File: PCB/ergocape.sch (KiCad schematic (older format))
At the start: 90 parts, among them J1 AudioJack4, J2 AudioJack4, SW1 SW_PUSH, U1 ATMEGA32U4, X1 Crystal_GND24_Small

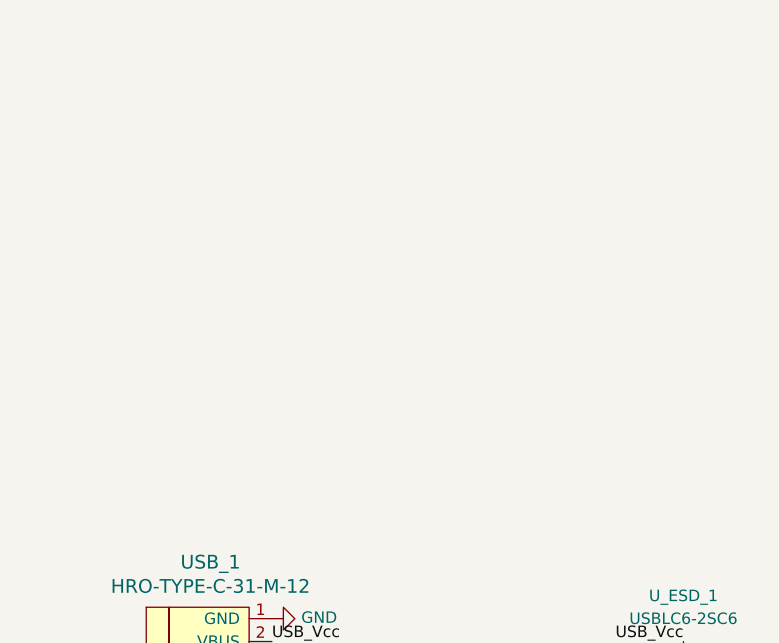
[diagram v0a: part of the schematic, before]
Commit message: added files for case files based of fr4 or similar.
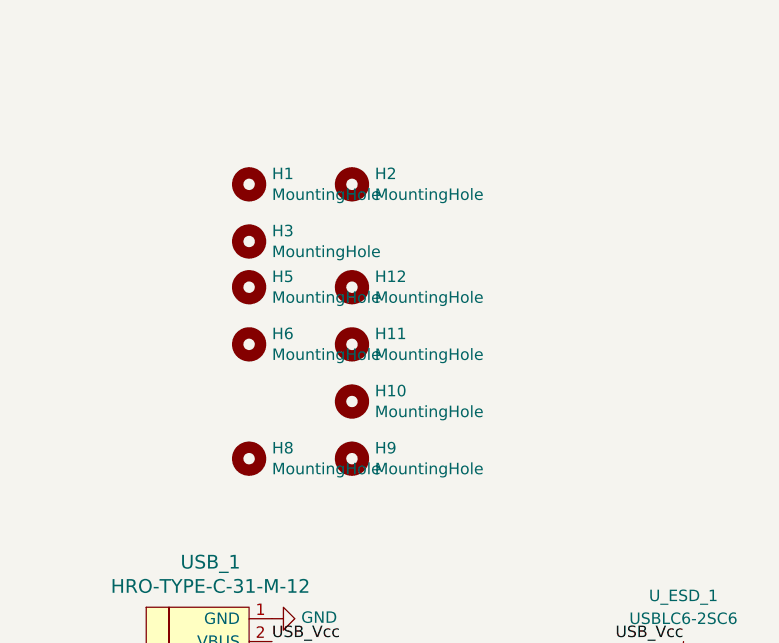
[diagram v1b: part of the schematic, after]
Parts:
- added H1, H10, H11, H12, H2, H3, H5, H6, H8, H9: MountingHole, usbc_footprint:mounting_hole_4.7x5.2mm, symbol Mechanical:MountingHole
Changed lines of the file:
@@
 $EndComp
 $Comp
-L power:GND #PWR?
+L power:GND #PWR0101
 U 1 1 5E0EA927
 P 8700 4250
-F 0 "#PWR?" H 8700 4000 50  0001 C CNN
+F 0 "#PWR0101" H 8700 4000 50  0001 C CNN
 F 1 "GND" H 8705 4077 50  0000 C CNN
 F 2 "" H 8700 4250 50  0001 C CNN
@@
 	4500 2900 4500 3400
 $Comp
-L power:GND #PWR?
+L power:GND #PWR0127
 U 1 1 5E1077CE
 P 2900 7500
-F 0 "#PWR?" H 2900 7250 50  0001 C CNN
+F 0 "#PWR0127" H 2900 7250 50  0001 C CNN
 F 1 "GND" V 2905 7372 50  0000 R CNN
 F 2 "" H 2900 7500 50  0001 C CNN
@@
 	1    0    0    -1
 $EndComp
+$Comp
+L Mechanical:MountingHole H5
+U 1 1 5E126410
+P 1000 4950
+F 0 "H5" H 1100 4996 50  0000 L CNN
+F 1 "MountingHole" H 1100 4905 50  0000 L CNN
+F 2 "usbc_footprint:mounting_hole_4.7x5.2mm" H 1000 4950 50  0001 C CNN
+F 3 "~" H 1000 4950 50  0001 C CNN
+	1    1000 4950
+	1    0    0    -1
+$EndComp
+$Comp
+L Mechanical:MountingHole H12
+U 1 1 5E12675F
+P 1450 4950
+F 0 "H12" H 1550 4996 50  0000 L CNN
+F 1 "MountingHole" H 1550 4905 50  0000 L CNN
+F 2 "usbc_footprint:mounting_hole_4.7x5.2mm" H 1450 4950 50  0001 C CNN
+F 3 "~" H 1450 4950 50  0001 C CNN
+	1    1450 4950
+	1    0    0    -1
+$EndComp
+$Comp
+L Mechanical:MountingHole H6
+U 1 1 5E12F4CE
+P 1000 5200
+F 0 "H6" H 1100 5246 50  0000 L CNN
+F 1 "MountingHole" H 1100 5155 50  0000 L CNN
+F 2 "usbc_footprint:mounting_hole_4.7x5.2mm" H 1000 5200 50  0001 C CNN
+F 3 "~" H 1000 5200 50  0001 C CNN
+	1    1000 5200
+	1    0    0    -1
+$EndComp
+$Comp
+L Mechanical:MountingHole H11
+U 1 1 5E12F4D5
+P 1450 5200
+F 0 "H11" H 1550 5246 50  0000 L CNN
+F 1 "MountingHole" H 1550 5155 50  0000 L CNN
+F 2 "usbc_footprint:mounting_hole_4.7x5.2mm" H 1450 5200 50  0001 C CNN
+F 3 "~" H 1450 5200 50  0001 C CNN
+	1    1450 5200
+	1    0    0    -1
+$EndComp
+$Comp
+L Mechanical:MountingHole H10
+U 1 1 5E138366
+P 1450 5450
+F 0 "H10" H 1550 5496 50  0000 L CNN
+F 1 "MountingHole" H 1550 5405 50  0000 L CNN
+F 2 "usbc_footprint:mounting_hole_4.7x5.2mm" H 1450 5450 50  0001 C CNN
+F 3 "~" H 1450 5450 50  0001 C CNN
+	1    1450 5450
+	1    0    0    -1
+$EndComp
+$Comp
+L Mechanical:MountingHole H8
+U 1 1 5E13836D
+P 1000 5700
+F 0 "H8" H 1100 5746 50  0000 L CNN
+F 1 "MountingHole" H 1100 5655 50  0000 L CNN
+F 2 "usbc_footprint:mounting_hole_4.7x5.2mm" H 1000 5700 50  0001 C CNN
+F 3 "~" H 1000 5700 50  0001 C CNN
+	1    1000 5700
+	1    0    0    -1
+$EndComp
+$Comp
+L Mechanical:MountingHole H9
+U 1 1 5E138374
+P 1450 5700
+F 0 "H9" H 1550 5746 50  0000 L CNN
+F 1 "MountingHole" H 1550 5655 50  0000 L CNN
+F 2 "usbc_footprint:mounting_hole_4.7x5.2mm" H 1450 5700 50  0001 C CNN
+F 3 "~" H 1450 5700 50  0001 C CNN
+	1    1450 5700
+	1    0    0    -1
+$EndComp
+$Comp
+L Mechanical:MountingHole H1
+U 1 1 5E1411A4
+P 1000 4500
+F 0 "H1" H 1100 4546 50  0000 L CNN
+F 1 "MountingHole" H 1100 4455 50  0000 L CNN
+F 2 "usbc_footprint:mounting_hole_4.7x5.2mm" H 1000 4500 50  0001 C CNN
+F 3 "~" H 1000 4500 50  0001 C CNN
+	1    1000 4500
+	1    0    0    -1
+$EndComp
+$Comp
+L Mechanical:MountingHole H2
+U 1 1 5E1411AB
+P 1450 4500
+F 0 "H2" H 1550 4546 50  0000 L CNN
+F 1 "MountingHole" H 1550 4455 50  0000 L CNN
+F 2 "usbc_footprint:mounting_hole_4.7x5.2mm" H 1450 4500 50  0001 C CNN
+F 3 "~" H 1450 4500 50  0001 C CNN
+	1    1450 4500
+	1    0    0    -1
+$EndComp
+$Comp
+L Mechanical:MountingHole H3
+U 1 1 5E1411B2
+P 1000 4750
+F 0 "H3" H 1100 4796 50  0000 L CNN
+F 1 "MountingHole" H 1100 4705 50  0000 L CNN
+F 2 "usbc_footprint:mounting_hole_4.7x5.2mm" H 1000 4750 50  0001 C CNN
+F 3 "~" H 1000 4750 50  0001 C CNN
+	1    1000 4750
+	1    0    0    -1
+$EndComp

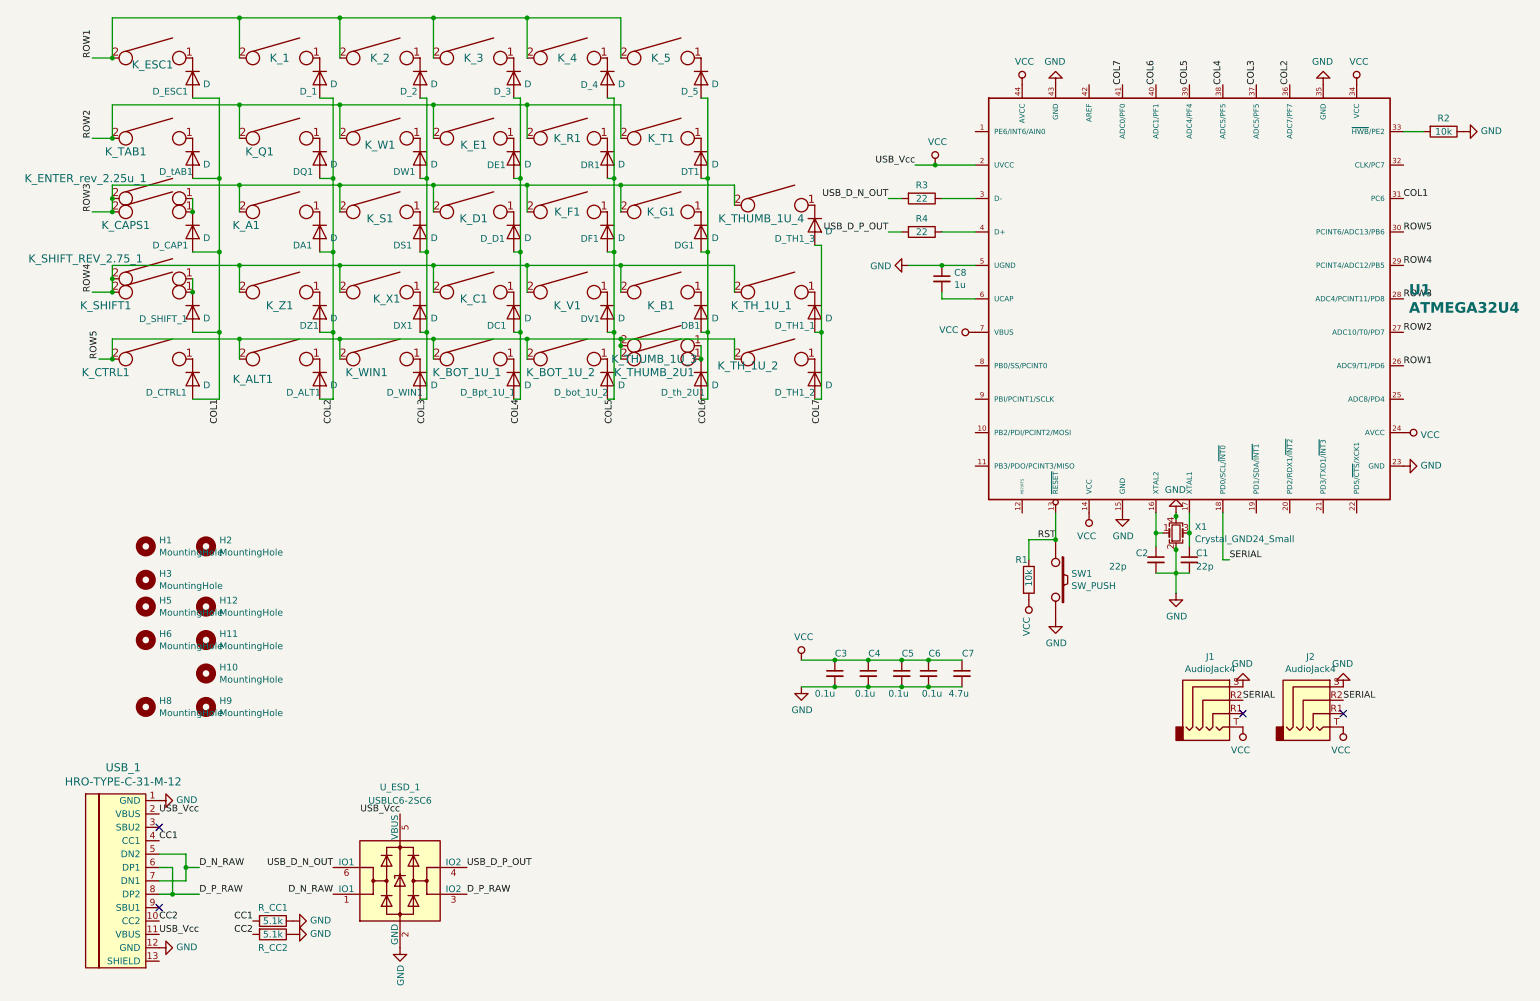
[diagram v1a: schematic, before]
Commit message: Change in layout and design, remove atmega32u4
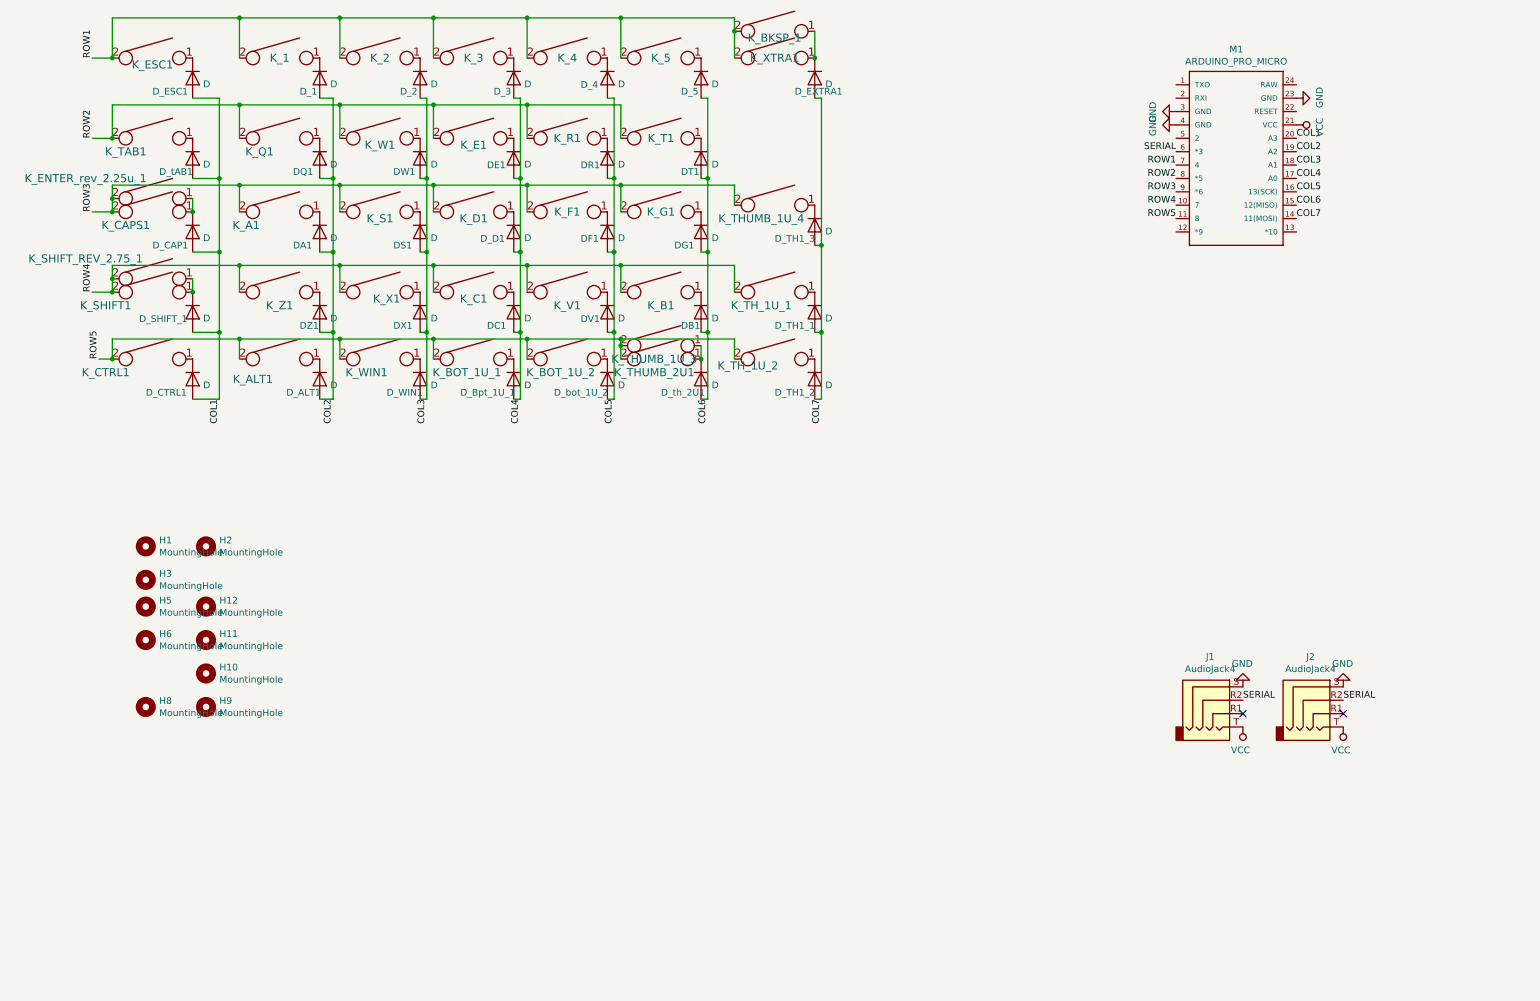
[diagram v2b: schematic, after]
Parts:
- removed C1, C2: 22p, Capacitor_SMD:C_0805_2012Metric_Pad1.15x1.40mm_HandSolder, symbol Device:C_Small
- removed C3, C4, C5, C6: 0.1u, Capacitor_SMD:C_0805_2012Metric_Pad1.15x1.40mm_HandSolder, symbol Device:C_Small
- removed C7: 4.7u, Capacitor_SMD:C_0805_2012Metric_Pad1.15x1.40mm_HandSolder, symbol Device:C_Small
- removed C8: 1u, Capacitor_SMD:C_0805_2012Metric_Pad1.15x1.40mm_HandSolder, symbol Device:C_Small
- removed R1, R2: 10k, Resistor_SMD:R_0805_2012Metric_Pad1.15x1.40mm_HandSolder, symbol Device:R
- removed R3, R4: 22, Resistor_SMD:R_0805_2012Metric_Pad1.15x1.40mm_HandSolder, symbol Device:R
- removed R_CC1, R_CC2: 5.1k, Resistor_SMD:R_0805_2012Metric_Pad1.15x1.40mm_HandSolder, symbol Device:R
- removed SW1: SW_PUSH, Button_Switch_SMD:SW_SPST_TL3342, symbol keyboard_parts:SW_PUSH
- removed U1: ATMEGA32U4, acheron_Components:TQPF-44_10x10mm_P0.8mm, symbol ergocape-rescue:ATMEGA32U4-acheronSymbols
- removed USB_1: HRO-TYPE-C-31-M-12, usbc_footprint:HRO-TYPE-C-31-M-12, symbol Type-C:HRO-TYPE-C-31-M-12
- removed U_ESD_1: USBLC6-2SC6, Package_TO_SOT_SMD:SOT-23-6, symbol Power_Protection_esd:USBLC6-2SC6
- removed X1: Crystal_GND24_Small, acheron_Components:Crystal_SMD_5032-4Pin-HandSolder, symbol Device:Crystal_GND24_Small
- added D_EXTRA1: D, Keebio-Parts:Diode-dual, symbol Device:D
- added K_BKSP_1: KEYSW, Keebio-Parts:Hybrid_PCB_200H-dual, symbol keyboard_parts:KEYSW
- added K_XTRA1: KEYSW, Keebio-Parts:Hybrid_PCB_100H_Dual_hole, symbol keyboard_parts:KEYSW
- added M1: ARDUINO_PRO_MICRO, SparkFun-Boards:ARDUINO_PRO_MICRO, symbol SparkFun-Boards:ARDUINO_PRO_MICRO
- H1, H10, H11, H12, H2, H3, H5, H6, H8, H9: footprint usbc_footprint:mounting_hole_4.7x5.2mm -> acheron_MountingHoles:MountingHole_2.5x4.0mm
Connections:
- net COL1: now also M1.20 (A3)
- net COL2: now also M1.19 (A2)
- net COL3: now also M1.18 (A1)
- net COL4: now also M1.17 (A0)
- net COL5: now also M1.16 (13(SCK))
- net COL6: now also M1.15 (12(MISO))
- net COL7: now also D_EXTRA1.2 (A), M1.14 (11(MOSI))
- net GND: now also M1.23 (GND), M1.3 (GND), M1.4 (GND)
- net ROW1: now also K_BKSP_1.2, K_XTRA1.2, M1.7 (4)
- net ROW2: now also M1.8 (*5)
- net ROW3: now also M1.9 (*6)
- net ROW4: now also M1.10 (7)
- net ROW5: now also M1.11 (8)
- net SERIAL: now also M1.6 (*3)
- net VCC: now also M1.21 (VCC)
- new net: D_EXTRA1.1 (K), K_BKSP_1.1, K_XTRA1.1
- no-connect marks 4 -> 2

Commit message: finalize plate and mounting holes
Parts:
- H1, H10, H11, H12, H2, H3, H5, H6, H8, H9: footprint acheron_MountingHoles:MountingHole_2.5x4.0mm -> usbc_footprint:mounting_hole_4.7x5.2mm
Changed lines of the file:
@@
 EESchema Schematic File Version 4
-LIBS:ergocape-cache
-EELAYER 26 0
+EELAYER 30 0
 EELAYER END
 $Descr A4 11693 8268
@@
 F 0 "H5" H 1100 4996 50  0000 L CNN
 F 1 "MountingHole" H 1100 4905 50  0000 L CNN
-F 2 "acheron_MountingHoles:MountingHole_2.5x4.0mm" H 1000 4950 50  0001 C CNN
+F 2 "usbc_footprint:mounting_hole_4.7x5.2mm" H 1000 4950 50  0001 C CNN
 F 3 "~" H 1000 4950 50  0001 C CNN
 	1    1000 4950
@@
 F 0 "H12" H 1550 4996 50  0000 L CNN
 F 1 "MountingHole" H 1550 4905 50  0000 L CNN
-F 2 "acheron_MountingHoles:MountingHole_2.5x4.0mm" H 1450 4950 50  0001 C CNN
+F 2 "usbc_footprint:mounting_hole_4.7x5.2mm" H 1450 4950 50  0001 C CNN
 F 3 "~" H 1450 4950 50  0001 C CNN
 	1    1450 4950
@@
 F 0 "H6" H 1100 5246 50  0000 L CNN
 F 1 "MountingHole" H 1100 5155 50  0000 L CNN
-F 2 "acheron_MountingHoles:MountingHole_2.5x4.0mm" H 1000 5200 50  0001 C CNN
+F 2 "usbc_footprint:mounting_hole_4.7x5.2mm" H 1000 5200 50  0001 C CNN
 F 3 "~" H 1000 5200 50  0001 C CNN
 	1    1000 5200
@@
 F 0 "H11" H 1550 5246 50  0000 L CNN
 F 1 "MountingHole" H 1550 5155 50  0000 L CNN
-F 2 "acheron_MountingHoles:MountingHole_2.5x4.0mm" H 1450 5200 50  0001 C CNN
+F 2 "usbc_footprint:mounting_hole_4.7x5.2mm" H 1450 5200 50  0001 C CNN
 F 3 "~" H 1450 5200 50  0001 C CNN
 	1    1450 5200
@@
 F 0 "H10" H 1550 5496 50  0000 L CNN
 F 1 "MountingHole" H 1550 5405 50  0000 L CNN
-F 2 "acheron_MountingHoles:MountingHole_2.5x4.0mm" H 1450 5450 50  0001 C CNN
+F 2 "usbc_footprint:mounting_hole_4.7x5.2mm" H 1450 5450 50  0001 C CNN
 F 3 "~" H 1450 5450 50  0001 C CNN
 	1    1450 5450
@@
 F 0 "H8" H 1100 5746 50  0000 L CNN
 F 1 "MountingHole" H 1100 5655 50  0000 L CNN
-F 2 "acheron_MountingHoles:MountingHole_2.5x4.0mm" H 1000 5700 50  0001 C CNN
+F 2 "usbc_footprint:mounting_hole_4.7x5.2mm" H 1000 5700 50  0001 C CNN
 F 3 "~" H 1000 5700 50  0001 C CNN
 	1    1000 5700
@@
 F 0 "H9" H 1550 5746 50  0000 L CNN
 F 1 "MountingHole" H 1550 5655 50  0000 L CNN
-F 2 "acheron_MountingHoles:MountingHole_2.5x4.0mm" H 1450 5700 50  0001 C CNN
+F 2 "usbc_footprint:mounting_hole_4.7x5.2mm" H 1450 5700 50  0001 C CNN
 F 3 "~" H 1450 5700 50  0001 C CNN
 	1    1450 5700
@@
 F 0 "H1" H 1100 4546 50  0000 L CNN
 F 1 "MountingHole" H 1100 4455 50  0000 L CNN
-F 2 "acheron_MountingHoles:MountingHole_2.5x4.0mm" H 1000 4500 50  0001 C CNN
+F 2 "usbc_footprint:mounting_hole_4.7x5.2mm" H 1000 4500 50  0001 C CNN
 F 3 "~" H 1000 4500 50  0001 C CNN
 	1    1000 4500
@@
 F 0 "H2" H 1550 4546 50  0000 L CNN
 F 1 "MountingHole" H 1550 4455 50  0000 L CNN
-F 2 "acheron_MountingHoles:MountingHole_2.5x4.0mm" H 1450 4500 50  0001 C CNN
+F 2 "usbc_footprint:mounting_hole_4.7x5.2mm" H 1450 4500 50  0001 C CNN
 F 3 "~" H 1450 4500 50  0001 C CNN
 	1    1450 4500
@@
 F 0 "H3" H 1100 4796 50  0000 L CNN
 F 1 "MountingHole" H 1100 4705 50  0000 L CNN
-F 2 "acheron_MountingHoles:MountingHole_2.5x4.0mm" H 1000 4750 50  0001 C CNN
+F 2 "usbc_footprint:mounting_hole_4.7x5.2mm" H 1000 4750 50  0001 C CNN
 F 3 "~" H 1000 4750 50  0001 C CNN
 	1    1000 4750
@@
 Connection ~ 6050 2250
 $Comp
-L power:VCC #PWR?
+L power:VCC #PWR0104
 U 1 1 5E1FE1EF
 P 9600 1350
-F 0 "#PWR?" H 9600 1200 50  0001 C CNN
+F 0 "#PWR0104" H 9600 1200 50  0001 C CNN
 F 1 "VCC" H 9618 1523 50  0000 C CNN
 F 2 "" H 9600 1350 50  0001 C CNN
